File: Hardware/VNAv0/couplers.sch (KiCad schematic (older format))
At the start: 4 parts

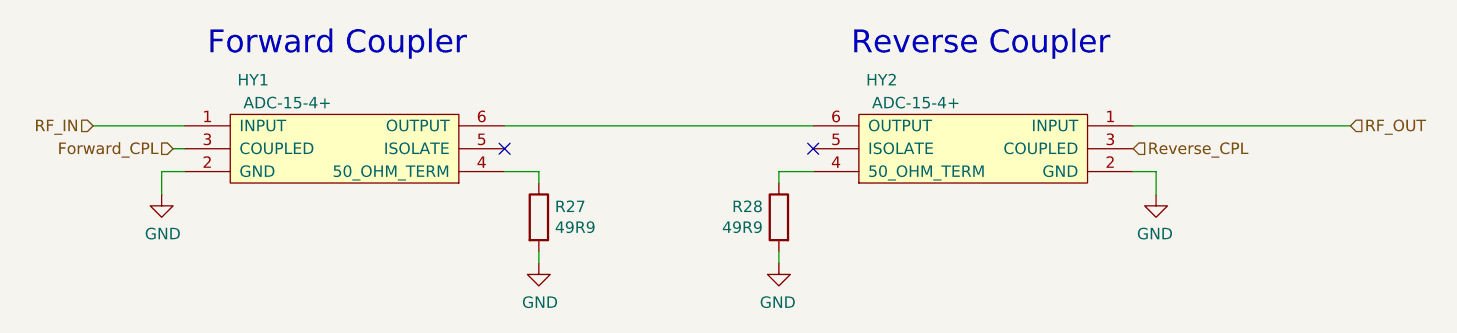
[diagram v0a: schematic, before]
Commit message: tx chain now works, however output power too low
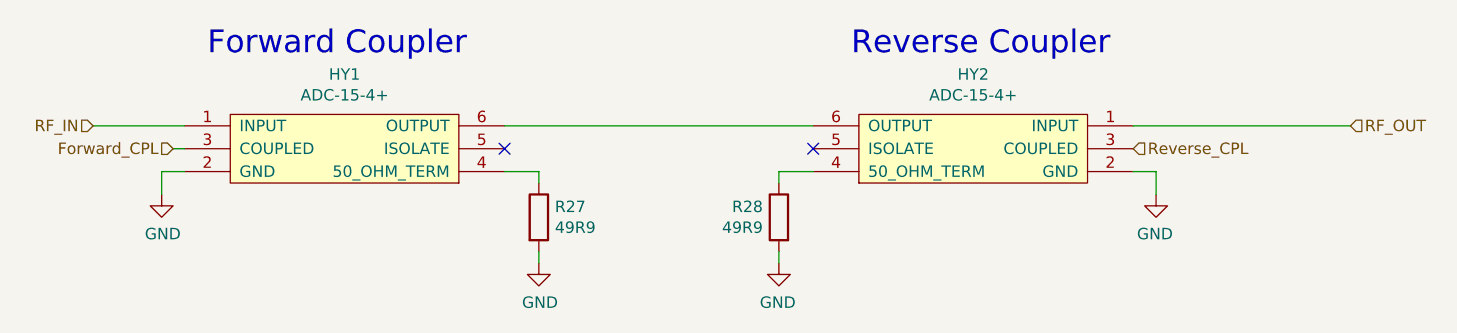
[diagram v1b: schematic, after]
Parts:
- HY1, HY2: footprint VNA_Footprints:CD542 -> (none)
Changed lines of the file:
@@
 Comment4 ""
 $EndDescr
-$Comp
-L VNA_Symbols:ADC-15-4+ HY1
-U 1 1 5C294AFE
-P 4050 1900
-F 0 "HY1" H 3700 2050 50  0000 C CNN
-F 1 "ADC-15-4+" H 3850 1950 50  0000 C CNN
-F 2 "VNA_Footprints:CD542" H 4050 1900 50  0001 C CNN
-F 3 "" H 4050 1900 50  0001 C CNN
-	1    4050 1900
-	1    0    0    -1
-$EndComp
 Wire Wire Line
 	3000 1950 3400 1950
@@
 Text Notes 3500 1650 0    100  ~ 0
 Forward Coupler
-$Comp
-L VNA_Symbols:ADC-15-4+ HY2
-U 1 1 5CC49764
-P 6900 1900
-F 0 "HY2" H 7350 2050 50  0000 C CNN
-F 1 "ADC-15-4+" H 7200 1950 50  0000 C CNN
-F 2 "VNA_Footprints:CD542" H 6900 1900 50  0001 C CNN
-F 3 "" H 6900 1900 50  0001 C CNN
-	1    6900 1900
-	-1   0    0    -1
-$EndComp
 Wire Wire Line
 	8500 1950 7550 1950
@@
 Text HLabel 8500 1950 2    50   Input ~ 0
 RF_OUT
+$Comp
+L VNA_Symbols:ADC-15-4+ HY1
+U 1 1 5D1726A9
+P 4050 1900
+F 0 "HY1" H 4100 2075 50  0000 C CNN
+F 1 "ADC-15-4+" H 4100 1984 50  0000 C CNN
+F 2 "" H 4050 1900 50  0001 C CNN
+F 3 "" H 4050 1900 50  0001 C CNN
+	1    4050 1900
+	1    0    0    -1
+$EndComp
+$Comp
+L VNA_Symbols:ADC-15-4+ HY2
+U 1 1 5D173678
+P 6900 1900
+F 0 "HY2" H 6950 2075 50  0000 C CNN
+F 1 "ADC-15-4+" H 6950 1984 50  0000 C CNN
+F 2 "" H 6900 1900 50  0001 C CNN
+F 3 "" H 6900 1900 50  0001 C CNN
+	1    6900 1900
+	-1   0    0    -1
+$EndComp
 $EndSCHEMATC
